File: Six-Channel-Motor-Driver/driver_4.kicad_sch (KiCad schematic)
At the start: 9 parts, among them J2 Screw_Terminal_01x02, Q1 Q_NMOS_GDS, Q2 Q_NMOS_GDS, Q3 Q_NMOS_GDS, Q4 Q_NMOS_GDS

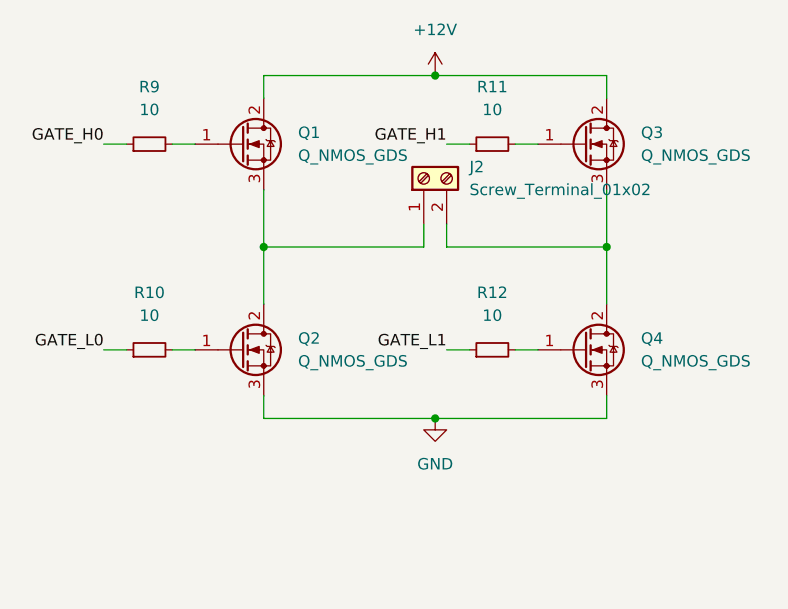
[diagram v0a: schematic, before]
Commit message: Added start of driver blocks
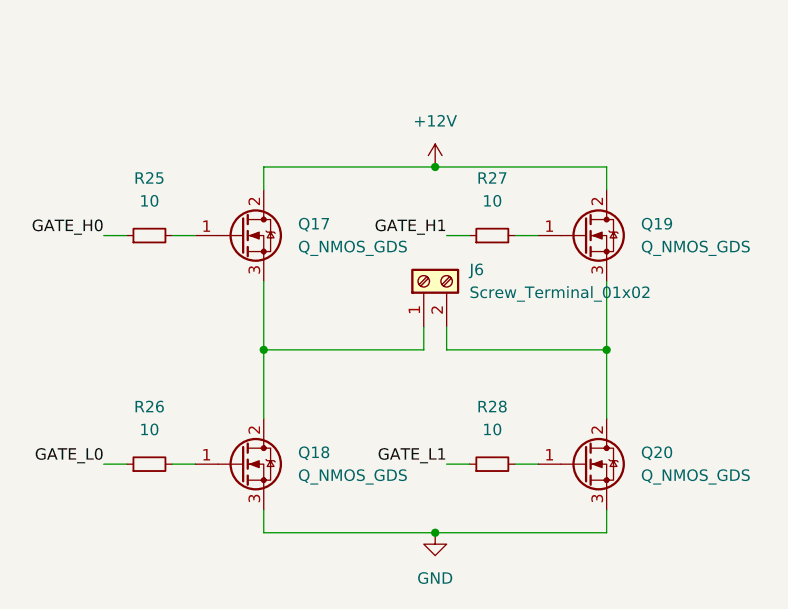
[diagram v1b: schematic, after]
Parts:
- removed J2: Screw_Terminal_01x02, Connector_Wire:SolderWire-2.5sqmm_1x02_P8.8mm_D2.4mm_OD4.4mm, symbol Connector:Screw_Terminal_01x02
- removed Q1, Q2, Q3, Q4: Q_NMOS_GDS, Package_TO_SOT_SMD:SOT-23, symbol Device:Q_NMOS_GDS
- removed R10, R11, R12, R9: 10, Resistor_SMD:R_0603_1608Metric, symbol Device:R_Small
- added J6: Screw_Terminal_01x02, Connector_Wire:SolderWire-2.5sqmm_1x02_P8.8mm_D2.4mm_OD4.4mm, symbol Connector:Screw_Terminal_01x02
- added Q17, Q18, Q19, Q20: Q_NMOS_GDS, Package_TO_SOT_SMD:SOT-23, symbol Device:Q_NMOS_GDS
- added R25, R26, R27, R28: 10, Resistor_SMD:R_0603_1608Metric, symbol Device:R_Small
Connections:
- net +12V: now also Q17.2 (D), Q19.2 (D)
- net GATE_H0: now also R25.1
- net GATE_H1: now also R27.1
- net GATE_L0: now also R26.1
- net GATE_L1: now also R28.1
- net GND: now also Q18.3 (S), Q20.3 (S)
- new net: Q18.1 (G), R26.2
- new net: Q17.1 (G), R25.2
- new net: J6.1 (Pin_1), Q17.3 (S), Q18.2 (D)
- new net: J6.2 (Pin_2), Q19.3 (S), Q20.2 (D)
- new net: Q20.1 (G), R28.2
- new net: Q19.1 (G), R27.2
